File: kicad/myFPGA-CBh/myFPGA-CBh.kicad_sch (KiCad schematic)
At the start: 62 parts, among them J1 Conn_01x04, J10 Conn_01x04, J11 Conn_01x04, J12 Conn_01x04, J13 Conn_01x04, J14 Conn_01x04, J15 Conn_01x04, J2 Conn_01x04, J3 Conn_01x04, J4 Conn_01x04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

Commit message: start new feature CE
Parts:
- added D16: LED (green), LED_SMD:LED_0805_2012Metric, symbol Device:LED
- added J16: Conn_01x02, Connector_PinHeader_2.54mm:PinHeader_1x02_P2.54mm_Horizontal, symbol Connector_Generic:Conn_01x02
- added R16: 330R, Resistor_SMD:R_0603_1608Metric, symbol Device:R
- added U10: BL1551B, Package_TO_SOT_SMD:SOT-363_SC-70-6, symbol Analog_Switch:NC7SB3157P6X
- U7, U8, U9: value NC7SB3157P6X -> BL1551B
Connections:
- net +3.3VP: now also U10.5 (V+)
- net GND: now also D16.1 (K), J16.1 (Pin_1), U10.2 (GND)
- net xp_ce: now reaches U2.7 (QH)
- net xp_ce: now also R16.1, U10.6
- net prio_0 renamed bus_4
- net bus_4: no longer U3.1 (I3)
- net prio_1 renamed bus_5
- net bus_5: now also U10.4; no longer U3.2 (I2)
- new net: D16.2 (A), R16.2
- new net ce: J16.2 (Pin_2), U10.1
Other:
- moved on the sheet: J10, J11, J12, J13, J14, J7, J8, J9

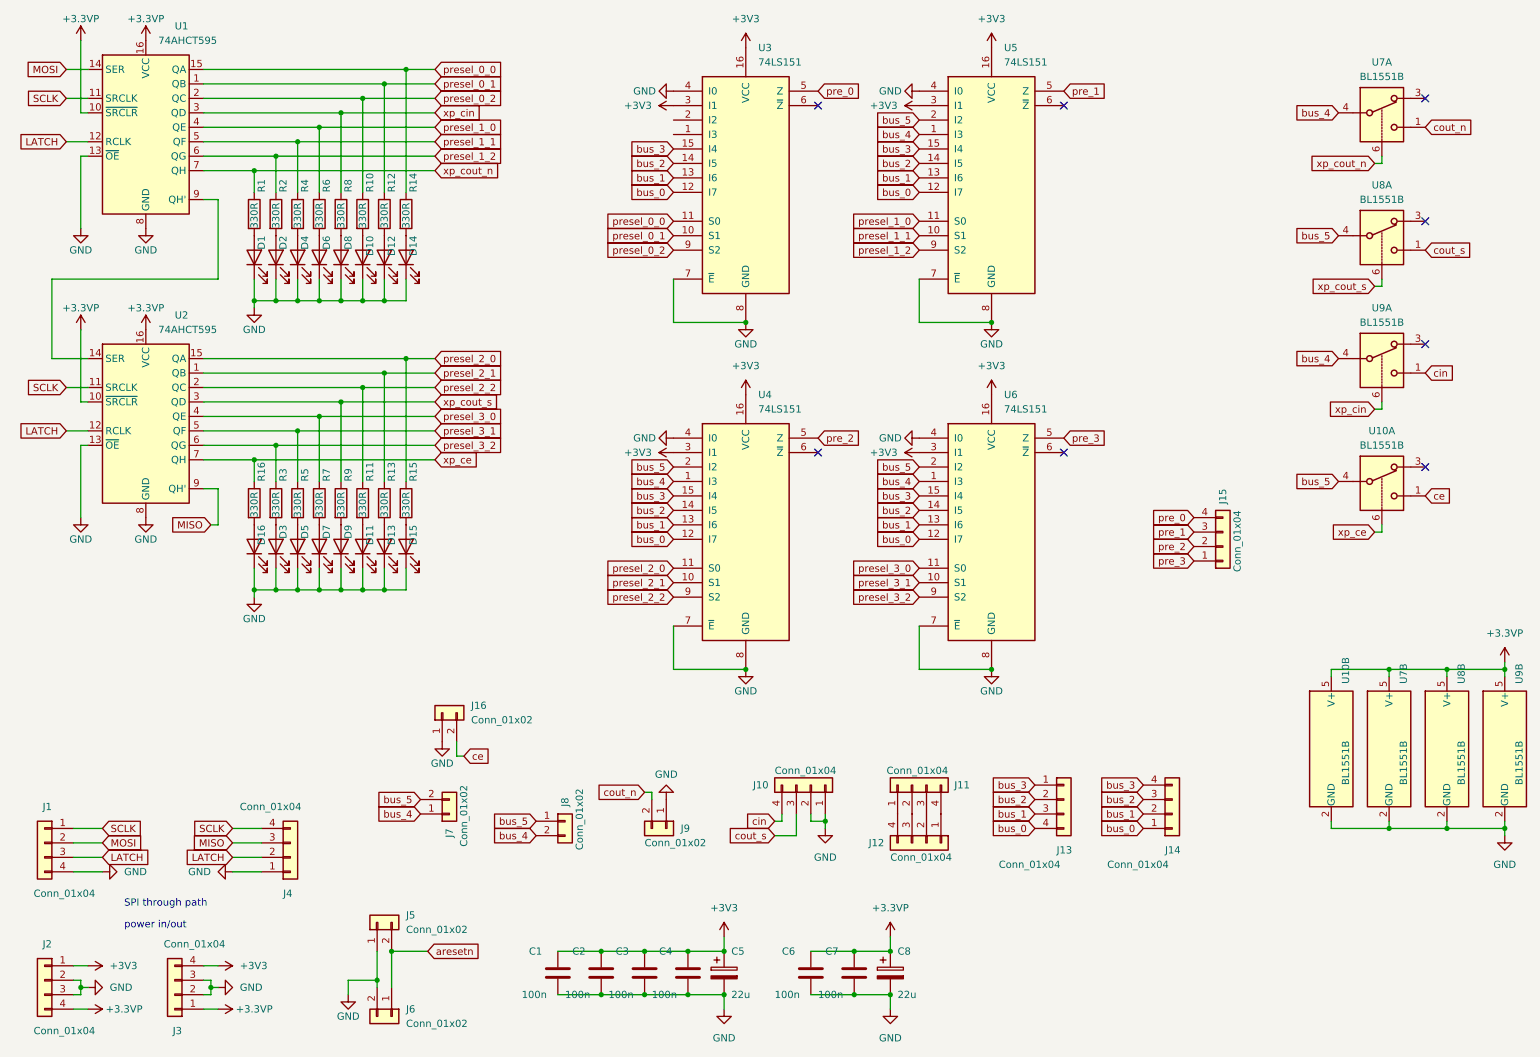
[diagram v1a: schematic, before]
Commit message: found more bugs
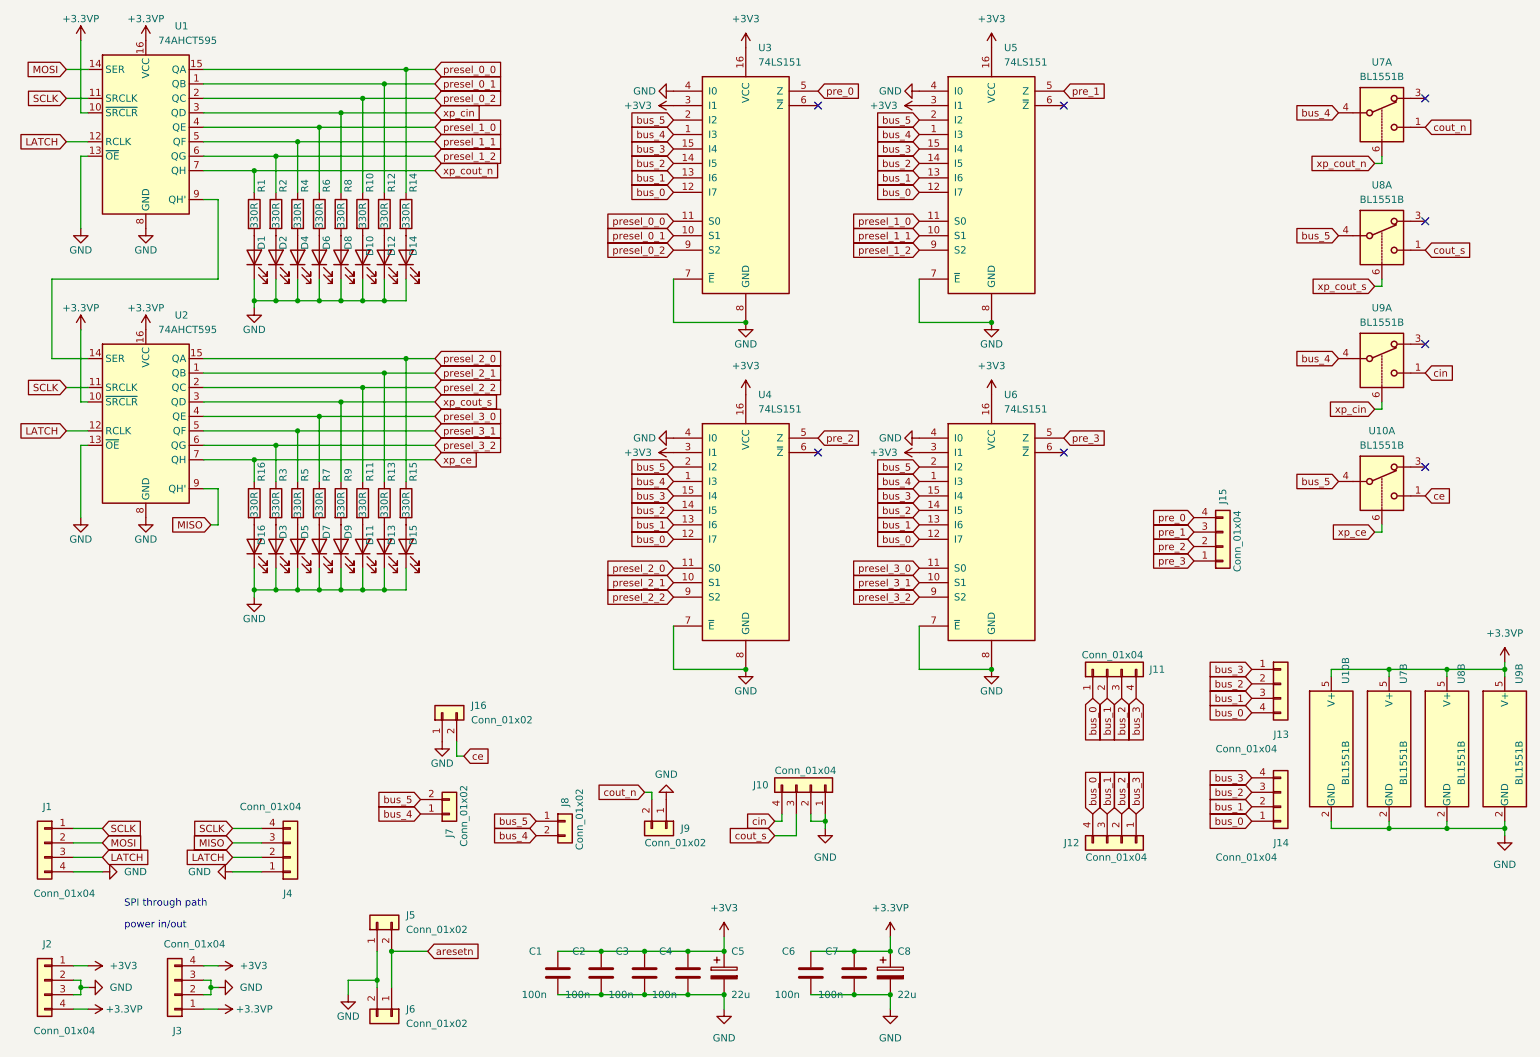
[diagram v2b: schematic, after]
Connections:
- net bus_0: now also J11.1 (Pin_1), J12.4 (Pin_4)
- net bus_1: now also J11.2 (Pin_2), J12.3 (Pin_3)
- net bus_2: now also J11.3 (Pin_3), J12.2 (Pin_2)
- net bus_3: now also J11.4 (Pin_4), J12.1 (Pin_1)
- net bus_4: now also U3.1 (I3)
- net bus_5: now also U3.2 (I2)
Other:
- moved on the sheet: J11, J12, J13, J14
